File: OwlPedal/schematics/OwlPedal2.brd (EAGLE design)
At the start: 103.1 x 79.5 mm, 88 parts, among them IC1 7805TV, IC6 TS924, J1 NEUTRIK_NMJ6HCD2, J2 NEUTRIK_NMJ6HCD2, J3 NEUTRIK_NMJ6HCD2, J4 NEUTRIK_NMJ6HCD2, J5 NEUTRIK_NMJ6HCD2, J6 NEUTRIK_NMJ6HCD2, J7 POWER_JACK, T1 BC846, T2 2N7002P

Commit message: routing, labels, moved headers to bottom
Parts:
- R25, R27: value 150R -> 1k
- moved R25 0.13 mm to (89.0, 15.6)
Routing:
- net +5V: track 162.0 -> 157.0 mm, vias 3 -> 2
- net A4: track 40.5 -> 37.2 mm, vias 2 -> 0
- net BYPASS: track 46.7 -> 44.9 mm, vias 1 -> 0
- net A3: track 38.5 -> 37.1 mm
- net GND: vias 73 -> 72
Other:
- outline, holes or cut-outs redrawn

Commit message: Rev02
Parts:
- moved R14 1.09 mm to (72.5, 39.3)
- moved R16 1.09 mm to (72.5, 35.8)
- moved C11 0.97 mm to (70.4, 35.8)
- moved R18 0.97 mm to (70.4, 39.3)
- moved R17 0.52 mm to (68.5, 37.3)
- moved C10 0.40 mm to (66.7, 37.3)
- moved R19 0.40 mm to (67.4, 40.5)
- moved C12 0.38 mm to (70.9, 47.6)
- moved R6 0.38 mm to (67.4, 53.7)
- moved C7 0.18 mm to (64.9, 37.3)
- moved C5 0.13 mm to (56.7, 36.8)
- moved C8 0.13 mm to (59.2, 36.2)
- moved R39 0.13 mm to (63.2, 37.3)
- moved R5 0.13 mm to (63.8, 40.5)
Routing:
- net N$37: track 21.9 -> 23.1 mm
- net CS_VREF: track 42.9 -> 41.9 mm
- net AOUT_A+: track 38.8 -> 39.8 mm
- net AOUT_B-: track 34.2 -> 33.3 mm
- net DC_IN_L: track 52.9 -> 53.7 mm
- net N$19: track 5.45 -> 6.20 mm
- net IN_R: track 46.7 -> 47.2 mm
- net GND: track 1.48 -> 1.47 mm, vias 72 -> 76

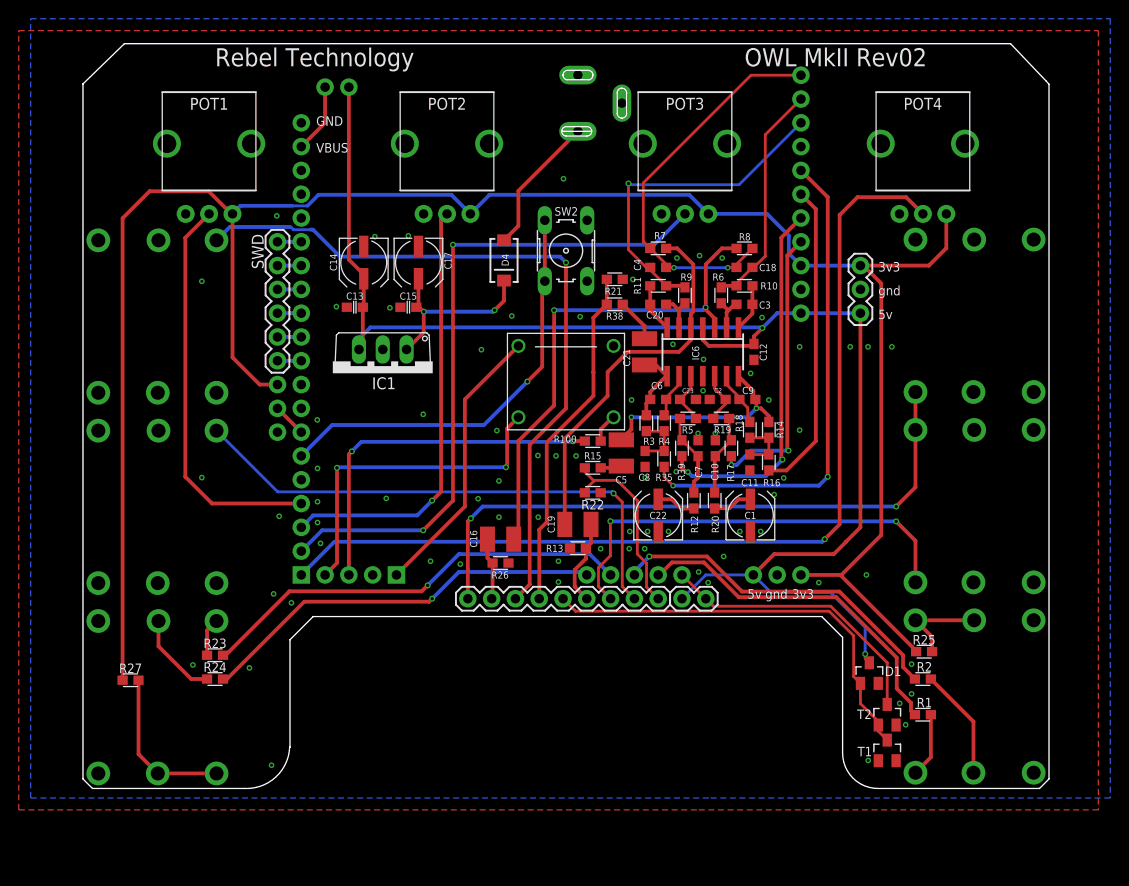
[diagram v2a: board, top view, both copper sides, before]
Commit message: part renamed/dnp
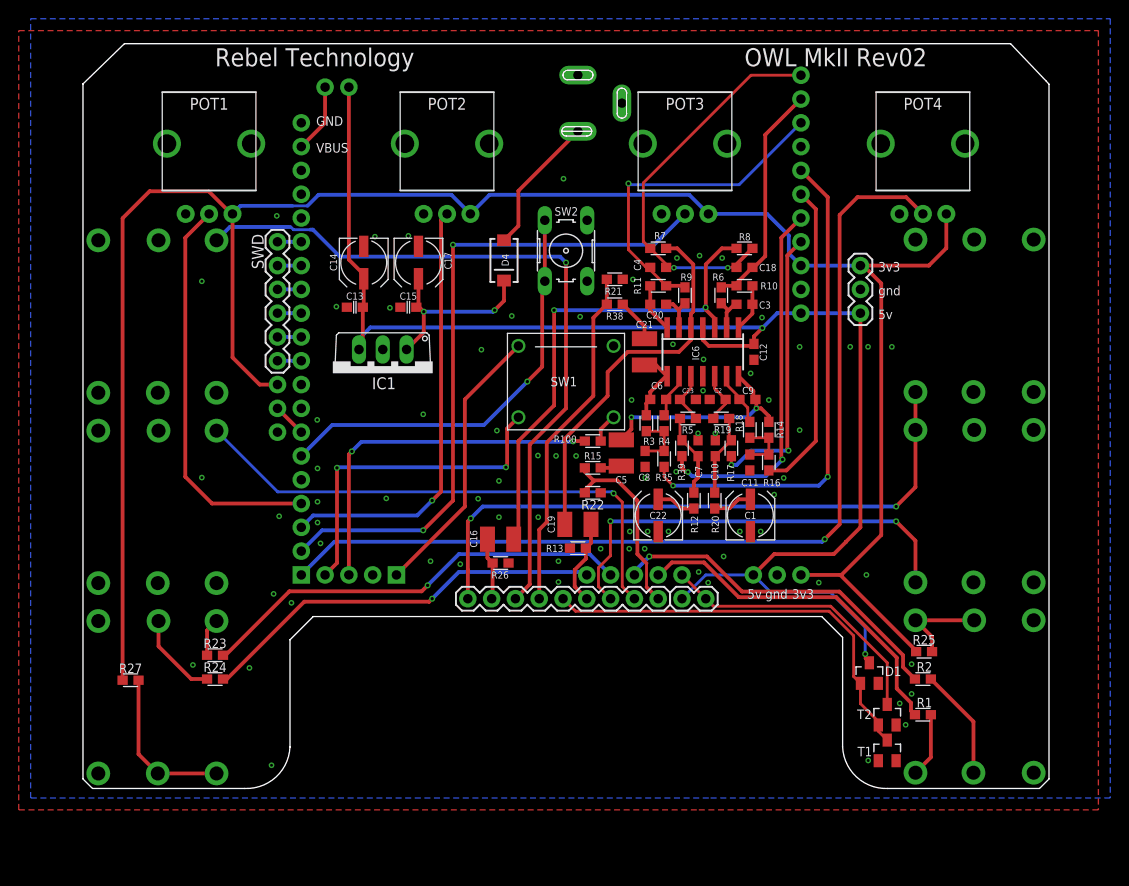
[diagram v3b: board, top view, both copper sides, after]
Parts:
- JP3: value M09 -> DNP
- JP6, SWD: value (none) -> DNP
- renumbered U$1 to SW1
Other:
- outline, holes or cut-outs redrawn
- board text added: "SW1"
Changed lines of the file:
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@@
 <wire x1="-0.762" y1="2.032" x2="0.254" y2="1.016" width="0.0254" layer="20"/>
 <wire x1="0.254" y1="1.016" x2="16.51" y2="1.016" width="0.0254" layer="20"/>
-<wire x1="16.51" y1="1.016" x2="21.30198125" y2="5.42698125" width="0.0254" layer="20" curve="90"/>
-<wire x1="21.30198125" y1="5.42698125" x2="21.336" y2="5.42698125" width="0.0254" layer="20"/>
-<wire x1="21.336" y1="5.42698125" x2="21.336" y2="16.891" width="0.0254" layer="20"/>
+<wire x1="16.51" y1="1.016" x2="21.336" y2="5.461" width="0.0254" layer="20" curve="90"/>
+<wire x1="21.336" y1="5.461" x2="21.336" y2="5.42698125" width="0.0254" layer="20"/>
+<wire x1="21.336" y1="5.42698125" x2="21.336" y2="5.461" width="0.0254" layer="20"/>
+<wire x1="21.336" y1="5.461" x2="21.336" y2="16.891" width="0.0254" layer="20"/>
 <wire x1="21.336" y1="16.891" x2="23.8125" y2="19.3675" width="0.0254" layer="20"/>
 <wire x1="23.8125" y1="19.3675" x2="78.105" y2="19.3675" width="0.0254" layer="20"/>
 <wire x1="78.105" y1="19.3675" x2="80.3275" y2="17.145" width="0.0254" layer="20"/>
-<wire x1="80.3275" y1="17.145" x2="80.3275" y2="4.79198125" width="0.0254" layer="20"/>
-<wire x1="80.3275" y1="4.79198125" x2="84.10348125" y2="1.016" width="0.0254" layer="20" curve="90"/>
-<wire x1="84.10348125" y1="1.016" x2="101.346" y2="1.016" width="0.0254" layer="20"/>
+<wire x1="80.3275" y1="17.145" x2="80.3275" y2="5.461" width="0.0254" layer="20"/>
+<wire x1="80.3275" y1="5.461" x2="85.1535" y2="1.016" width="0.0254" layer="20" curve="90"/>
+<wire x1="85.1535" y1="1.016" x2="101.346" y2="1.016" width="0.0254" layer="20"/>
 <wire x1="101.346" y1="1.016" x2="102.362" y2="2.032" width="0.0254" layer="20"/>
 <wire x1="102.362" y1="2.032" x2="102.362" y2="76.2" width="0.0254" layer="20"/>
@@
 <text x="26.455" y="74.0975" size="1.016" layer="22" font="vector" rot="MR180">5V</text>
 <dimension x1="3.81" y1="80.518" x2="3.81" y2="1.016" x3="-8.954053125" y3="40.767" textsize="1.778" layer="47"/>
+<text x="49.149" y="43.942" size="1.016" layer="25">SW1</text>
 </plain>
 <attributes>
@@
 <attribute name="VALUE" x="88.265" y="3.81" size="1.27" layer="27" ratio="10"/>
 </element>
-<element name="U$1" library="SWITCH-5GTH9" package="5GTH9" value="5GTH9" x="50.8" y="44.45" locked="yes" smashed="yes"/>
+<element name="SW1" library="SWITCH-5GTH9" package="5GTH9" value="5GTH9" x="50.8" y="44.45" locked="yes" smashed="yes"/>
 <element name="R1" library="Rebel" package="0603" value="150R" x="88.9" y="8.89" smashed="yes" rot="R180">
 <attribute name="NAME" x="88.2269" y="9.6774" size="1.016" layer="25" font="vector"/>
@@
 <attribute name="VALUE" x="91.44" y="11.4046" size="1.016" layer="27" font="vector" ratio="10" rot="R180"/>
 </element>
-<element name="JP3" library="SparkFun" package="1X09" value="M09" x="40.3225" y="21.2725" smashed="yes">
+<element name="JP3" library="SparkFun" package="1X09" value="DNP" x="40.3225" y="21.2725" smashed="yes">
 <attribute name="VALUE" x="39.0525" y="18.0975" size="1.27" layer="27"/>
 </element>
@@
 <attribute name="VALUE" x="16.8275" y="37.7825" size="1.27" layer="28" rot="MR90"/>
 </element>
-<element name="SWD" library="SparkFun" package="1X06" value="" x="20.0025" y="59.3725" smashed="yes" rot="R270">
+<element name="SWD" library="SparkFun" package="1X06" value="DNP" x="20.0025" y="59.3725" smashed="yes" rot="R270">
 <attribute name="NAME" x="17.2593" y="60.2107" size="1.27" layer="25" ratio="10" rot="R270"/>
 <attribute name="VALUE" x="16.8275" y="60.6425" size="1.27" layer="27" rot="R270"/>
@@
 </element>
 <element name="C21" library="Rebel" package="C1210" value="1u Film" x="59.182" y="47.625" smashed="yes" rot="R90">
-<attribute name="NAME" x="57.658" y="46.99" size="0.762" layer="25" font="vector" rot="R90" align="bottom-center"/>
+<attribute name="NAME" x="59.182" y="50.165" size="0.762" layer="25" font="vector" align="bottom-center"/>
 </element>
 <element name="C22" library="Rebel" package="CPOL-5" value="22u" x="60.6425" y="30.1625" smashed="yes" rot="R90">
@@
 </element>
 <element name="C23" library="resistor" package="C0603" value="1n C0G" x="63.8175" y="42.545" smashed="yes" rot="R180">
-<attribute name="NAME" x="63.205390625" y="43.217753125" size="0.508" layer="25"/>
+<attribute name="NAME" x="63.205390625" y="43.217753125" size="0.508" layer="25" font="vector"/>
 <attribute name="VALUE" x="64.7065" y="44.577" size="1.27" layer="27" rot="R180"/>
 </element>
@@
 <attribute name="VALUE" x="44.45" y="78.6465" size="0.4064" layer="28" rot="MR0"/>
 </element>
-<element name="JP6" library="SparkFun" package="1X02" value="" x="63.1825" y="21.2725" smashed="yes">
+<element name="JP6" library="SparkFun" package="1X02" value="DNP" x="63.1825" y="21.2725" smashed="yes">
 <attribute name="VALUE" x="135.89" y="59.055" size="1.27" layer="27" rot="R180"/>
 </element>
@@
 <contactref element="T1" pad="1"/>
 <contactref element="J5" pad="S"/>
-<contactref element="U$1" pad="1"/>
+<contactref element="SW1" pad="1"/>
 <contactref element="J3" pad="TN"/>
 <contactref element="JP4" pad="2"/>
@@
 <contactref element="R15" pad="2"/>
 <contactref element="R22" pad="1"/>
-<wire x1="60.6425" y1="21.2725" x2="59.3979" y2="22.5171" width="0.3048" layer="1"/>
-<wire x1="59.3979" y1="25.0571" x2="58.42" y2="26.035" width="0.3048" layer="1"/>
+<wire x1="60.6425" y1="21.2725" x2="59.3979" y2="22.5171" width="0.4064" layer="1"/>
+<wire x1="59.3979" y1="25.0571" x2="58.42" y2="26.035" width="0.4064" layer="1"/>
 <wire x1="59.3979" y1="22.5171" x2="59.3979" y2="25.0571" width="0.3048" layer="1"/>
-<wire x1="58.42" y1="26.035" x2="58.42" y2="31.75" width="0.3048" layer="1"/>
-<wire x1="58.42" y1="31.75" x2="56.261" y2="33.909" width="0.3048" layer="1"/>
-<wire x1="56.261" y1="33.909" x2="53.848" y2="33.909" width="0.3048" layer="1"/>
+<wire x1="58.42" y1="26.035" x2="58.42" y2="31.75" width="0.4064" layer="1"/>
+<wire x1="58.42" y1="31.75" x2="56.261" y2="33.909" width="0.4064" layer="1"/>
+<wire x1="56.261" y1="33.909" x2="53.848" y2="33.909" width="0.4064" layer="1"/>
 <wire x1="53.848" y1="33.909" x2="53.7845" y2="33.8455" width="0.3048" layer="1"/>
-<wire x1="53.7845" y1="33.8455" x2="52.8075" y2="32.8685" width="0.3048" layer="1"/>
-<wire x1="52.8075" y1="32.8685" x2="52.8075" y2="32.5755" width="0.3048" layer="1"/>
-<wire x1="52.8075" y1="34.8225" x2="53.7845" y2="33.8455" width="0.3048" layer="1"/>
-<wire x1="52.8075" y1="35.2425" x2="52.8075" y2="34.8225" width="0.3048" layer="1"/>
+<wire x1="53.7845" y1="33.8455" x2="52.8075" y2="32.8685" width="0.4064" layer="1"/>
+<wire x1="52.8075" y1="32.8685" x2="52.8075" y2="32.5755" width="0.4064" layer="1"/>
+<wire x1="52.8075" y1="34.8225" x2="53.7845" y2="33.8455" width="0.4064" layer="1"/>
+<wire x1="52.8075" y1="35.2425" x2="52.8075" y2="34.8225" width="0.4064" layer="1"/>
 </signal>
 <signal name="OUT_L">
@@
 </signal>
 <signal name="N$10">
-<contactref element="U$1" pad="+3"/>
+<contactref element="SW1" pad="+3"/>
 <contactref element="R100" pad="1"/>
 <wire x1="55.88" y1="40.64" x2="55.7775" y2="40.64" width="0.4064" layer="1"/>
@@
 <wire x1="47.9425" y1="28.64355" x2="48.7479" y2="29.44895" width="0.4064" layer="1"/>
 <wire x1="48.7479" y1="29.44895" x2="48.7479" y2="37.9529" width="0.4064" layer="1"/>
-<wire x1="53.7354" y1="45.42605" x2="53.721" y2="45.44045" width="0.4064" layer="1"/>
-<wire x1="53.7354" y1="42.9404" x2="53.7354" y2="45.42605" width="0.4064" layer="1"/>
-<wire x1="48.7479" y1="37.9529" x2="53.7354" y2="42.9404" width="0.4064" layer="1"/>
+<wire x1="53.721" y1="42.926" x2="53.721" y2="51.269" width="0.4064" layer="1"/>
+<wire x1="48.7479" y1="37.9529" x2="53.721" y2="42.926" width="0.4064" layer="1"/>
 <wire x1="53.721" y1="51.269" x2="55.157" y2="52.705" width="0.4064" layer="1"/>
-<wire x1="53.721" y1="45.44045" x2="53.721" y2="51.269" width="0.4064" layer="1"/>
 <wire x1="55.157" y1="52.705" x2="55.157" y2="55.372" width="0.4064" layer="1"/>
 </signal>
@@
 </signal>
 <signal name="A22">
-<contactref element="U$1" pad="4"/>
+<contactref element="SW1" pad="4"/>
 <contactref element="EXTSPI" pad="4"/>
 <wire x1="25.0825" y1="23.8125" x2="26.3525" y2="25.0825" width="0.4064" layer="1"/>
@@
 </signal>
 <signal name="A25">
-<contactref element="U$1" pad="-2"/>
+<contactref element="SW1" pad="-2"/>
 <contactref element="EXTSPI" pad="1"/>
 <wire x1="32.7025" y1="23.8125" x2="40.005" y2="31.115" width="0.4064" layer="1"/>
@@
 <wire x1="61.4925" y1="56.974" x2="59.7925" y2="58.674" width="0.3048" layer="1"/>
 <wire x1="69" y1="56.642" x2="69" y2="56.974" width="0.3048" layer="1"/>
-<wire x1="70.7" y1="58.674" x2="69" y2="56.974" width="0.3048" layer="1"/>
+<wire x1="70.7" y1="58.674" x2="69" y2="56.974" width="0.4064" layer="1"/>
 <via x="68.072" y="56.6055" extent="1-16" drill="0.3048"/>
 <via x="62.3205" y="56.6055" extent="1-16" drill="0.3048"/>
@@
 <wire x1="69" y1="54.6735" x2="67.5395" y2="54.6735" width="0.4064" layer="1"/>
 <wire x1="67.3735" y1="54.5075" x2="67.5395" y2="54.6735" width="0.3048" layer="1"/>
-<wire x1="70.7" y1="56.642" x2="69" y2="54.942" width="0.3048" layer="1"/>
+<wire x1="70.7" y1="56.642" x2="69" y2="54.942" width="0.4064" layer="1"/>
 <wire x1="69" y1="54.6735" x2="69" y2="54.942" width="0.3048" layer="1"/>
 <contactref element="ANG3" pad="4"/>
-<wire x1="75.8825" y1="74.6125" x2="72.0725" y2="70.8025" width="0.3048" layer="1"/>
-<wire x1="72.0725" y1="70.8025" x2="72.0725" y2="57.8485" width="0.3048" layer="1"/>
-<wire x1="72.0725" y1="57.8485" x2="70.866" y2="56.642" width="0.3048" layer="1"/>
+<wire x1="75.8825" y1="74.6125" x2="72.0725" y2="70.8025" width="0.4064" layer="1"/>
+<wire x1="72.0725" y1="70.8025" x2="72.0725" y2="57.8485" width="0.4064" layer="1"/>
+<wire x1="72.0725" y1="57.8485" x2="70.866" y2="56.642" width="0.4064" layer="1"/>
 <wire x1="70.866" y1="56.642" x2="70.7" y2="56.642" width="0.3048" layer="1"/>
 </signal>

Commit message: OWL Pedal mkII Rev03
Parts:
- removed ADC1, EXTSPI: (no value), SparkFun:1X04
- removed D4: S1J, SparkFun:SMA-DIODE
- removed IC6: TS924, linear:SO14
- removed LGP1-5: (no value), SparkFun:1X05
- removed PWR: (no value), SparkFun:1X02
- removed R100: 150R, Rebel:0603
- removed R35: 5k1, Rebel:0603
- removed R38: 22R, Rebel:0603
- removed R39: 1k, Rebel:0603
- removed T1: BC846, NXP_60_26022015:SOT23
- removed T2: 2N7002P, NXP_60_26022015:SOT23
- added C24: 10n Film, Rebel:C1210
- added JP1: (no value), SparkFun:1X03
- added JP2: (no value), SparkFun:1X04
- added R28, R29: 1k, Rebel:0603
- added R30, R31, R32: 150R, Rebel:0603
- added U1: TS5A22364, Rebel:DGS0010A_L
- added U2: (no value), Hangar:TSR-1-2450
- C1: value 22u -> 100n; device Rebel:CPOL-5 -> Rebel:C0603
- C10: value 4n7 C0G -> 1u Film; device resistor:C0603 -> Rebel:C1210
- C11, C8: value 2n2 C0G -> 220p C0G
- C12: value 100n -> 1n C0G
- C13: value 100n -> 1n C0G; device Rebel:C0603 -> resistor:C0603
- C14: value 22u -> 100n; device Rebel:CPOL-5 -> resistor:C0603
- C15: value 100n 16v -> 220p C0G; device Rebel:C0603 -> resistor:C0603
- C16: value 1u Film -> 10n; device Rebel:C1210 -> Rebel:C0603
- C17: value 10u -> 2n2 C0G; device Rebel:CPOL-5 -> resistor:C0603
- C18, C4: value 2n2 C0G -> 22u; device resistor:C0603 -> Rebel:CPOL-5
- C19: value 1u Film -> 4n7 C0G; device Rebel:C1210 -> resistor:C0603
- C2: value 1n C0G -> 22u; device resistor:C0603 -> Rebel:CPOL-5
- C20: value 220p C0G -> 4n7 C0G
- C21: value 1u Film -> 22u; device Rebel:C1210 -> Rebel:CPOL-5
- C22: value 22u -> 2n2 C0G; device Rebel:CPOL-5 -> resistor:C0603
- C23: value 1n C0G -> 10n Film; device resistor:C0603 -> Rebel:C1210
- C3: value 220p C0G -> 100n 16v; device resistor:C0603 -> Rebel:C0603
- C5: value 1u Film -> 2n2 C0G; device Rebel:C1210 -> resistor:C0603
- C7: value 4n7 C0G -> 2n2 C0G
- C9: value 220p C0G -> 1u Film; device resistor:C0603 -> Rebel:C1210
- D1: value BAS16 -> S1J; device NXP_60_26022015:SOT23 -> SparkFun:SMA-DIODE
- IC1: value 7805TV -> TS924; device linear:TO220V -> linear:SO14
- JP3: value DNP -> 2X6 FEMALE; device SparkFun:1X09 -> SparkFun-Connectors:2X6
- JP5: device SparkFun:1X03 -> SparkFun:1X04
- JP6: value DNP -> (none); device SparkFun:1X02 -> SparkFun:1X04
- R1, R24: value 150R -> 1M
- R10: value 100R -> 5k1
- R11: value 100R -> 2k
- R13: value 1M -> 1k
- R14: value 5k1 -> 2k
- R15: value 22R -> 5k1
- R16: value 5k1 -> 100R
- R17: value 1k -> 100R
- R18: value 2k -> 5k1
- R2: value 150R -> 100R
- R21, R22: value 100k -> 1k
- R23: value 150R -> 5k1
- R25, R27, R5: value 1k -> 1M
- R26: value 1M -> 150R
- R3: value 5k1 -> 560R
- R4: value 2k -> 560R
- R6: value 560R -> 100R
- R7, R8: value 10k -> 100k
- R9: value 560R -> 150R
- SW1: value 5GTH9 -> (none); device SWITCH-5GTH9:5GTH9 -> switch-omron:B3F-10XX
- SW2: value (none) -> 5GTH9; device switch-omron:B3F-10XX -> SWITCH-5GTH9:5GTH9
- moved J1 96.6 mm to (94.6, 10.8), turned to 180 degrees
- moved J4 87.6 mm to (6.99, 31.1), turned to 0 degrees
- moved R24 78.6 mm to (90.2, 29.2), turned to 180 degrees
- moved R27 75.0 mm to (78.7, 21.6), turned to 270 degrees
- moved R23 62.7 mm to (72.6, 35.8), turned to 90 degrees
- moved D1 58.8 mm to (44.2, 57.4), turned to 270 degrees
- moved R1 57.2 mm to (60.6, 58.7)
- moved R2 50.6 mm to (60.6, 54.7)
- moved C1 47.7 mm to (28.3, 52.4), turned to 180 degrees
- moved C14 43.2 mm to (70.9, 45.8)
- moved JP3 41.0 mm to (77.5, 3.81), turned to 90 degrees
- moved JP6 40.7 mm to (22.5, 23.8), flipped to the bottom, turned to 90 degrees
- moved J5 40.6 mm to (94.6, 51.4)
- moved J6 40.6 mm to (6.99, 51.4)
- moved C2 40.5 mm to (29.2, 57.1), turned to 270 degrees
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- renumbered ANG1 to JP7, ANG3 to JP9, SWD2 to JP10, TGP1-4 to JP8, USB1 to JP11
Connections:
- removed net A1: LGP1-5.1, R24.2
- removed net A16_SW2: JP8.4, SW2.1, SW2.2
- removed net A2: LGP1-5.2, R23.2
- removed net A5: JP6.2, LGP1-5.5, T2.3
- removed net N$38: C5.2, R15.1
- removed net USB_VBUS: JP11.4, PWR.2
- new net A16: JP8.4, SW2.-2
- new net FOOTSWITCH: C16.1, JP2.2, JP3.9, R27.2
- new net N$28: C11.2, IC1.8, R10.2, R17.2
- new net N$30: C9.1, U1.9
- new net N$32: C15.2, IC1.14, R15.2, R16.2
- net +3V3: now also JP1.3, R28.1, R29.1; no longer JP5.3, R25.1
- net +5V: now also C1.1, C14.1, C2.+, IC1.4, JP1.1, JP11.4, JP3.11, U1.1, U2.3; no longer C12.1, C13.1, C14.+, D1.3, IC1.3, IC6.4, JP5.1, JP6.1, PWR.1
- net +9V: now also D1.A; no longer D4.A
- net A13: now also SW1.1, SW1.2
- net A14: now also SW2.4
- net A17: now also R9.2
- net A18_ADC1: now also JP6.4; no longer ADC1.4
- net A19_ADC2: now also JP6.3; no longer ADC1.3
- net A20_ADC3: now also JP6.2; no longer ADC1.2
- net A21_ADC4: now also JP6.1; no longer ADC1.1
- net A22: now also JP5.4; no longer EXTSPI.4, SW1.4
- net A23: now also JP5.3, R26.2; no longer EXTSPI.3, R100.2
- net A24: now also JP5.2, R30.2; no longer EXTSPI.2
- net A25: now also JP5.1, U1.5, U1.7; no longer EXTSPI.1, SW1.-2
- net A3: now also JP2.3, R32.2; no longer LGP1-5.3, R2.2
- net A4: now also JP2.4, R31.2; no longer LGP1-5.4, R1.2
- net AIN_A: now also C7.1, R4.1, U1.4; no longer C18.1, R10.1
- net AIN_B: now also C5.1, R2.1, R3.1, U1.8; no longer C4.1, R11.1, R9.1
- net AOUT_A+: now also R19.1; no longer R39.1
- net AOUT_A-: now also R18.1; no longer R35.1
- net AOUT_B+: now also R22.1; no longer R17.1
- net AOUT_B-: now also R23.1; no longer R16.1
- net BYPASS: now also JP2.1, JP3.10; no longer D1.1, JP3.5, T1.3, T2.1
- net CS_VREF: now also C5.2, C7.2, R1.2, R5.2; no longer C18.2, C4.2, R7.2, R8.2
- net DC_IN_L: now also C24.1, IC1.3, R5.1; no longer C16.1, IC6.3, R8.1
- net DC_IN_R: now also C23.1, IC1.5, R1.1; no longer C19.1, IC6.5, R7.1
- net FX_IN_L: now also C24.2, R25.1; no longer C16.2, R26.1
- net FX_IN_R: now also C23.2, R24.1; no longer C19.2, R13.1
- net FX_OUT_L: now also C10.2, JP3.3, R8.1; no longer JP3.4, R21.1, R38.2
- net FX_OUT_R: now also C9.2, JP3.7, R7.1; no longer JP3.9, R15.2, R22.1
- net GND: now also C1.2, C12.1, C13.1, C14.2, C16.2, C17.2, C18.-, C19.2, C2.-, C20.2, C21.-, C22.2, C3.2, C4.-, IC1.11, J5.TN, JP1.2, JP3.12, R24.2, R25.2, R7.2, R8.2, SW1.3, SW1.4, SW2.1, U1.6, U2.2; no longer C1.-, C10.2, C11.2, C12.2, C13.2, C14.-, C15.2, C17.-, C2.1, C22.-, C23.1, C7.2, C8.2, IC1.2, IC6.11, J3.TN, JP5.2, R13.2, R21.2, R22.2, R26.2, SW1.1, SW2.3, SW2.4, T1.1, T2.2
- net IN_L: now also J3.TN, J5.T; no longer J3.T, J4.TN
- net IN_R: now also J3.T, JP3.5; no longer J4.T, JP3.7
- net N$1: now also J1.RN, J1.TN, R28.2; no longer J5.RN, J5.TN, R25.2
- net N$10: now also R9.1, SW2.+3; no longer R100.1, SW1.+3
- net N$11: now also R17.1, U1.2; no longer C21.1, C6.2, IC6.8, R3.2
- net N$12: now also J1.R, R31.1; no longer J5.R, R2.1
- net N$13: now also C17.1, R10.1, R11.1, R18.2; no longer C8.1, R3.1, R35.2, R4.1
- net N$14: now also C6.1, IC1.6, R3.2; no longer C20.1, IC6.6, R9.2
- net N$15: now also J1.T, R32.1; no longer J5.T, R1.1
- net N$16: now also C11.1, IC1.9, R11.2; no longer C6.1, IC6.9, R4.2
- net N$17: now also C12.2, IC1.10, R12.2; no longer C23.2, IC6.10, R5.2
- net N$18: now also C19.1, R12.1, R19.2, R20.2; no longer C7.1, R12.2, R39.2, R5.1
- net N$19: now also C15.1, IC1.13, R14.2; no longer C9.1, IC6.13, R18.2
- net N$2: now also J2.R, R30.1; no longer J6.R, R24.1
- net N$20: now also C13.2, IC1.12, R13.2; no longer C2.2, IC6.12, R19.2
- net N$21: now also C20.1, R13.1, R21.2, R22.2; no longer C10.1, R17.2, R19.1, R20.2
- net N$22: now also C8.1, IC1.2, R4.2; no longer C3.1, IC6.2, R6.2
- net N$23: now also C8.2, IC1.1, R6.2; no longer C3.2, IC6.1, R10.2
- net N$24: now also C22.1, R15.1, R23.2; no longer C11.1, R16.2, R18.1
- net N$25: now also C6.2, IC1.7, R2.2; no longer C20.2, IC6.7, R11.2
- net N$26: now also J2.T, R26.1; no longer J6.T, R23.1
- net N$27: now also C10.1, U1.3; no longer C21.2, R38.1
- net N$29: now also C18.+, R20.1; no longer C22.+, R12.1
- net N$31: now also C21.+, R21.1; no longer C1.+, R20.1
- net N$37: now also R16.1, U1.10; no longer C5.1, C9.2, IC6.14, R14.2
- net N$4: now also J2.RN, J2.TN, R29.2; no longer J6.RN, J6.TN, R27.2
- net N$51: now also C3.1, C4.+, D1.C, U2.1; no longer C15.1, C17.+, D4.C, IC1.1
- net OUT_L: now also J6.T, JP3.4; no longer J1.T, JP3.3
- net OUT_R: now also J4.T; no longer J2.T
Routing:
- net A25: track 29.8 -> 104.5 mm, vias 0 -> 4
- net FX_IN_L: track 6.62 -> 55.3 mm, vias 0 -> 1
- net AIN_A: track 24.6 -> 72.1 mm
- net A2: track 46.8 -> 0.00 mm, vias 1 -> 0
- net A16_SW2: track 45.4 -> 0.00 mm, vias 1 -> 0
- net AIN_B: track 36.1 -> 81.4 mm
- net N$28: track 0.00 -> 45.2 mm, vias 0 -> 2
- net A1: track 43.7 -> 0.00 mm, vias 1 -> 0
- net A13: track 0.00 -> 42.4 mm, vias 0 -> 1
- net FX_OUT_L: track 37.1 -> 77.2 mm, vias 0 -> 1
- net A22: track 35.9 -> 0.00 mm, vias 2 -> 0
- net FOOTSWITCH: track 0.00 -> 35.0 mm
- net A17: track 0.00 -> 34.1 mm, vias 0 -> 1
- net A16: track 0.00 -> 33.3 mm, vias 0 -> 1
- net FX_OUT_R: track 20.4 -> 53.4 mm, vias 0 -> 1
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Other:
- outline, holes or cut-outs redrawn
- board text added: "OWL Pedal MkII Rev03"
- board text removed: "5V"
- board text removed: "OWL MkII Rev02"
